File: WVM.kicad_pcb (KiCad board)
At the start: 2 copper layers, 31 parts, among them J1 USB4215-03-A_REVA, P1 S2B-PH-SM4-TB, Q1 BSS138, Q2 BSS138, SW1 SW_SPST, SW2 SW_SPST, U1 NORA-W106-00B, U2 CH340C, U3 IIS3DWBTR, U4 TPS63036YFGT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

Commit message: 09/08/2025
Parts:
- added H1: MountingHole, MountingHole:MountingHole_2.2mm_M2, F.Cu at (188.0, 83.0)
- added H2: MountingHole, MountingHole:MountingHole_2.2mm_M2, F.Cu at (213.5, 83.0)
- added H3: MountingHole, MountingHole:MountingHole_2.2mm_M2, F.Cu at (188.0, 116.5)
- added H4: MountingHole, MountingHole:MountingHole_2.2mm_M2, F.Cu at (213.5, 116.5)
- C2, C6: moved to B.Cu
- moved R2 52.0 mm to (206.5, 105.5)
- moved C2 50.3 mm to (122.5, 102.5), turned to -90 degrees
- moved R1 49.4 mm to (204.0, 105.5)
- moved C6 40.8 mm to (132.0, 106.5), turned to 180 degrees
- moved R4 40.1 mm to (192.0, 90.0), turned to 90 degrees
- moved R5 39.9 mm to (192.0, 92.5), turned to -90 degrees
- moved R3 38.3 mm to (193.0, 107.0), turned to 180 degrees
- moved C4 36.7 mm to (211.5, 112.5), turned to -90 degrees
- moved L1 35.8 mm to (190.0, 93.0)
- moved D2 30.4 mm to (206.5, 108.0), turned to -90 degrees
- moved C7 28.1 mm to (200.9, 107.5), turned to 180 degrees
- moved D1 27.2 mm to (204.0, 108.0), turned to -90 degrees
- moved C10 25.4 mm to (198.0, 104.5), turned to -90 degrees
- moved C1 24.0 mm to (194.5, 86.5), turned to 90 degrees
- moved C11 23.5 mm to (194.0, 90.0), turned to 90 degrees
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
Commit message: 10-10-2025
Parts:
- moved C2 37.6 mm to (160.0, 99.2), turned to 90 degrees
- moved C4 31.5 mm to (204.9, 81.6)
- moved C3 29.5 mm to (205.0, 87.0)
- moved P1 28.9 mm to (155.9, 90.5), turned to -90 degrees
- moved U2 27.2 mm to (155.0, 102.2), turned to 180 degrees
- moved SW2 24.1 mm to (190.5, 99.2)
- moved C6 23.6 mm to (153.0, 95.7), turned to 0 degrees
- moved Q2 14.3 mm to (148.4, 103.4), turned to 180 degrees
- moved D2 14.2 mm to (202.0, 94.5), turned to 90 degrees
- moved Q1 14.0 mm to (148.4, 98.7), turned to 180 degrees
- moved D1 13.5 mm to (203.5, 94.5), turned to 90 degrees
- moved R3 11.3 mm to (200.7, 98.7), turned to -90 degrees
- moved H4 11.0 mm to (206.0, 108.5)
- moved SW1 10.8 mm to (190.5, 104.7)
- moved C10 10.1 mm to (196.5, 94.5), turned to 0 degrees
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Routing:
- net GND: track 0.00 -> 221.2 mm
- net +BAT: track 0.00 -> 72.9 mm
- net 3V3: track 0.00 -> 60.5 mm
- net BOOT: track 0.00 -> 58.7 mm
- net TX: track 0.00 -> 56.9 mm
- net RX: track 0.00 -> 50.7 mm
- net D-: track 0.00 -> 41.5 mm
- net D+: track 0.00 -> 40.7 mm
- net RESET: track 0.00 -> 31.5 mm
- net GPIO1: track 0.00 -> 21.2 mm
- net Net-(D1-A): track 0.00 -> 20.8 mm
- net Net-(Q1-G): track 0.00 -> 16.6 mm
- net (no net): track 0.00 -> 13.4 mm
- net Net-(Q1-S): track 0.00 -> 10.7 mm
- net EN: track 0.00 -> 6.67 mm
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
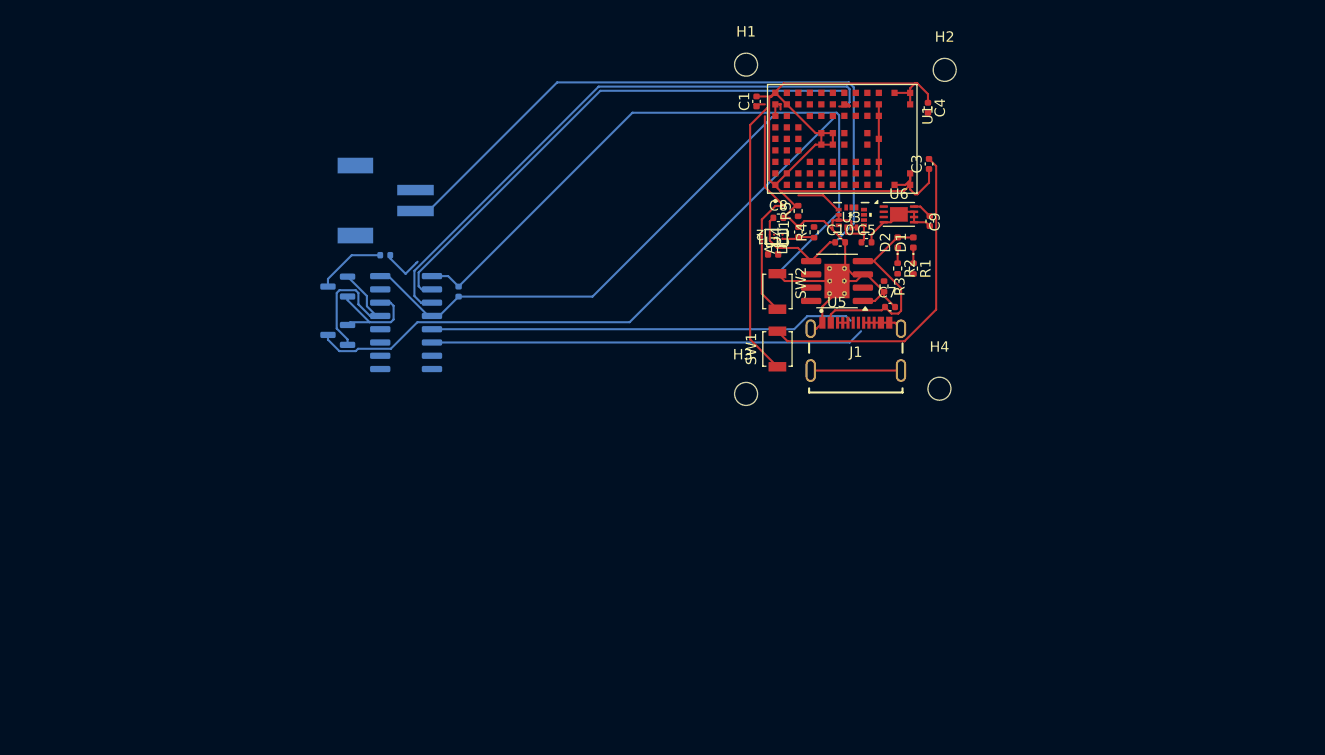
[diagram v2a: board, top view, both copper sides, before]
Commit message: Part Placement completed with board outline
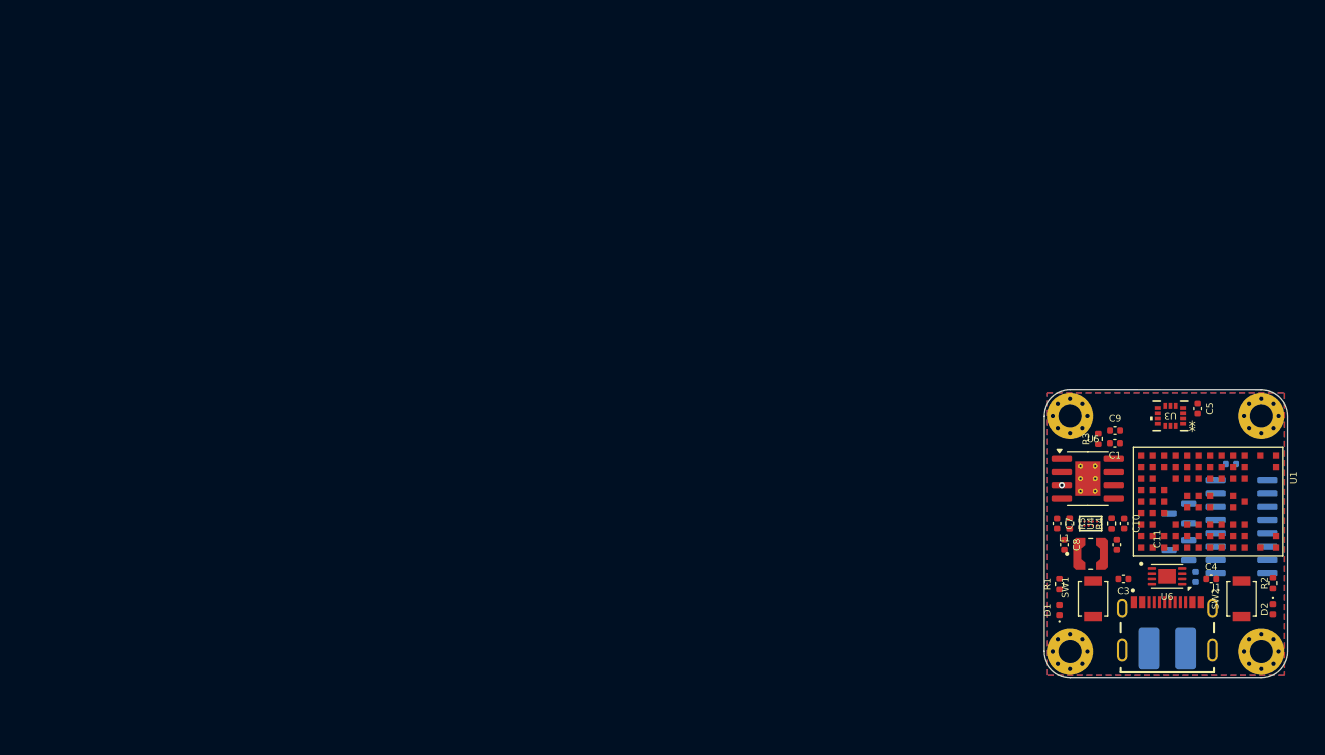
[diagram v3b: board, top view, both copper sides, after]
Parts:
- removed P1: S2B-PH-SM4-TB, S2B_PH_SM4_TB:JST_S2B-PH-SM4-TB
- added J2: Conn_01x02_Pin, Bat_pad:Untitled, B.Cu at (227.8, 130.8)
- H1, H2, H3, H4: footprint MountingHole:MountingHole_2.2mm_M2 -> MountingHole:MountingHole_2.2mm_M2_Pad_Via
- L1: value 1.5uH -> LPS3015-152MLC; footprint Inductor_SMD:L_0402_1005Metric -> LP3051:IND_LPS3015-152MLC
- moved Q1 84.3 mm to (228.9, 123.9)
- moved C6 83.4 mm to (230.5, 126.5), turned to -90 degrees
- moved U2 82.3 mm to (234.9, 121.7)
- moved Q2 82.3 mm to (228.9, 120.4)
- moved C2 75.7 mm to (233.9, 115.7), turned to 0 degrees
- moved H1 74.7 mm to (236.8, 133.6)
- moved SW2 53.3 mm to (234.9, 128.6), turned to 90 degrees
- moved C4 52.6 mm to (232.0, 126.7), turned to 0 degrees
- moved D2 50.2 mm to (237.9, 129.6), turned to -90 degrees
- moved U1 49.3 mm to (231.7, 119.3)
- moved C1 47.4 mm to (222.8, 113.7), turned to 180 degrees
- moved R2 46.8 mm to (237.9, 127.1)
- moved H2 44.9 mm to (236.8, 111.1)
- moved C3 43.8 mm to (223.6, 126.7), turned to 180 degrees
- moved U6 43.1 mm to (227.8, 126.5), turned to 180 degrees
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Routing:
- net GND: track 221.2 -> 0.00 mm, vias 0 -> 1
- net +BAT: track 72.9 -> 0.00 mm
- net 3V3: track 60.5 -> 0.00 mm
- net BOOT: track 58.7 -> 0.00 mm
- net TX: track 56.9 -> 0.00 mm
- net RX: track 50.7 -> 0.00 mm
- net D-: track 41.5 -> 0.00 mm
- net D+: track 40.7 -> 0.00 mm
- net RESET: track 31.5 -> 0.00 mm
- net GPIO1: track 21.2 -> 0.00 mm
- net Net-(D1-A): track 20.8 -> 0.00 mm
- net Net-(Q1-G): track 16.6 -> 0.00 mm
- net (no net): track 13.4 -> 0.00 mm
- net Net-(Q1-S): track 10.7 -> 0.00 mm
- net EN: track 6.67 -> 0.00 mm
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- added copper zone on F.Cu, net 3V3
- added copper zone on B.Cu, net GND
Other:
- board outline added: 23.3 x 27.6 mm

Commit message: 17102025
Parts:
- removed C2, C9: 0.1uF, Capacitor_SMD:C_0402_1005Metric
- removed C6: 1uF, Capacitor_SMD:C_0402_1005Metric
- removed Q1, Q2: BSS138, Package_TO_SOT_SMD:SOT-23
- removed U2: CH340C, Package_SO:SOIC-16_3.9x9.9mm_P1.27mm
- removed U6: MCP9808_DFN, Package_DFN_QFN:DFN-8-1EP_3x2mm_P0.5mm_EP1.7x1.4mm
- added J4: Conn_01x02_Pin, Connector_PinHeader_1.00mm:PinHeader_1x02_P1.00mm_Vertical, F.Cu at (237.8, 131.8)
- added J5: Conn_01x02_Pin, Connector_PinHeader_1.00mm:PinHeader_1x02_P1.00mm_Vertical, F.Cu at (237.8, 129.8)
- added J6: Conn_01x02_Pin, Connector_PinHeader_1.00mm:PinHeader_1x02_P1.00mm_Vertical, F.Cu at (237.8, 127.8)
- moved R2 20.0 mm to (218.5, 132.0), turned to 180 degrees
- moved D2 17.1 mm to (221.0, 132.0), turned to 0 degrees
- moved SW2 14.9 mm to (220.0, 128.0), turned to 0 degrees
- moved C4 8.84 mm to (223.2, 127.5), turned to -90 degrees
- moved C3 7.78 mm to (223.5, 134.5), turned to 90 degrees
- moved SW1 5.94 mm to (220.0, 134.5), turned to 0 degrees
- moved H4 5.38 mm to (218.5, 139.0)
- moved H1 5.21 mm to (237.0, 138.8)
- moved D1 3.72 mm to (221.1, 130.7), turned to 0 degrees
- moved R1 3.68 mm to (218.6, 130.7), turned to 180 degrees
- moved J1 2.58 mm to (230.2, 134.5)
- moved J2 2.58 mm to (230.2, 131.8)
- moved C5 2.42 mm to (232.5, 112.0)
- moved U3 2.36 mm to (229.8, 112.7)
- moved U1 1.24 mm to (232.0, 120.5)
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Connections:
- J1 pad A6: D+ -> unconnected-(J1-DP1-PadA6)
- J1 pad A7: D- -> unconnected-(J1-DN1-PadA7)
- J2 pad 2: -BAT -> GND
- U1 pad A2: SCL -> unconnected-(U1-FSPIWP/GPIO38-PadA2)
- U1 pad D3: SDA -> unconnected-(U1-FSPIHD/GPIO33-PadD3)
- U1 pad E7: unconnected-(U1-GPIO9-PadE7) -> INT2
- U1 pad H8: unconnected-(U1-GPIO2-PadH8) -> EN
- U1 pad H9: unconnected-(U1-GPIO8-PadH9) -> INT1
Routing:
- net GND: track 0.00 -> 148.3 mm, vias 1 -> 43
- net 3V3: track 0.00 -> 68.1 mm, vias 0 -> 7
- net Net-(D1-A): track 0.00 -> 29.6 mm
- net MISO: track 0.00 -> 29.5 mm, vias 0 -> 2
- net +BAT: track 0.00 -> 24.7 mm
- net RESET: track 0.00 -> 22.7 mm, vias 0 -> 3
- net RX: track 0.00 -> 22.1 mm, vias 0 -> 3
- net BOOT: track 0.00 -> 21.2 mm, vias 0 -> 2
- net Net-(U5-~{CHRG}): track 0.00 -> 18.7 mm, vias 0 -> 2
- net EN: track 0.00 -> 17.4 mm, vias 0 -> 2
- net GPIO1: track 0.00 -> 16.3 mm, vias 0 -> 2
- net Net-(U5-~{STDBY}): track 0.00 -> 15.6 mm, vias 0 -> 2
- net TX: track 0.00 -> 14.9 mm, vias 0 -> 2
- net CLK: track 0.00 -> 13.8 mm, vias 0 -> 2
- net MOSI: track 0.00 -> 11.8 mm, vias 0 -> 2
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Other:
- board size 23.3 x 27.6 mm -> 23.5 x 32.9 mm
